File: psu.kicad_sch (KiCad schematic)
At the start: 68 parts, among them J3 Screw_Terminal_01x03, J4 Screw_Terminal_01x02, U11 LM337_SOT223, U14 LM337_SOT223, U15 AP1117-ADJ, U18 AP1117-ADJ, U2 AP1117-ADJ

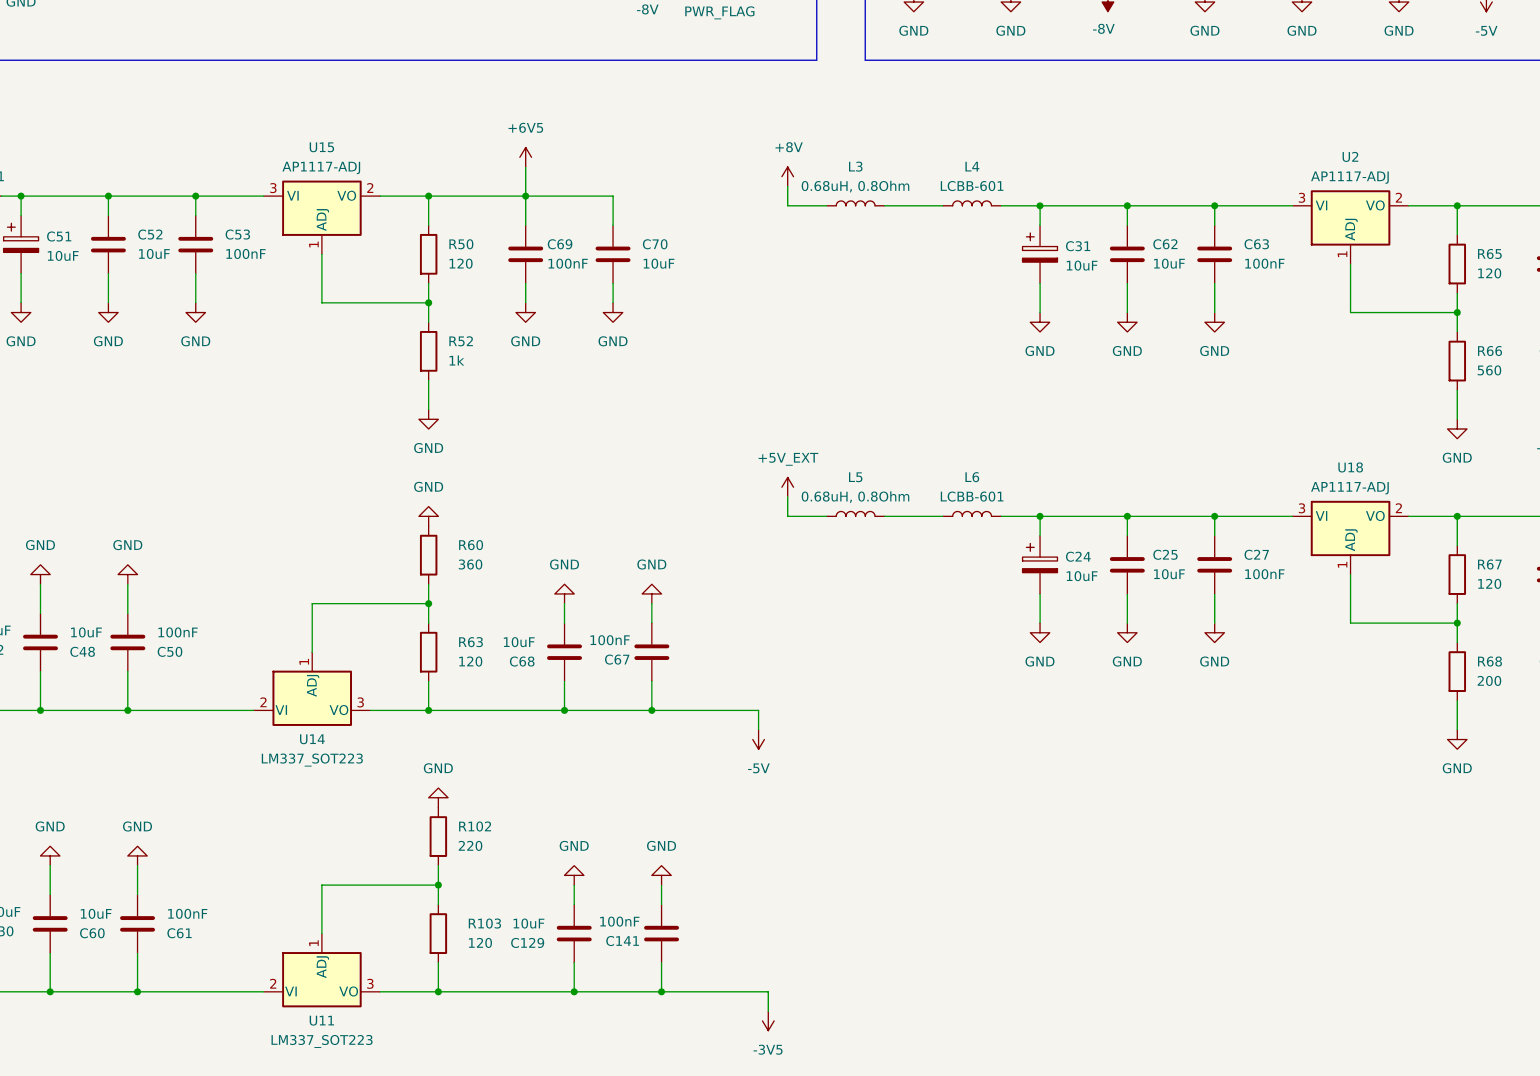
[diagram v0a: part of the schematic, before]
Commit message: Remove the stage between DAC and FET buffer
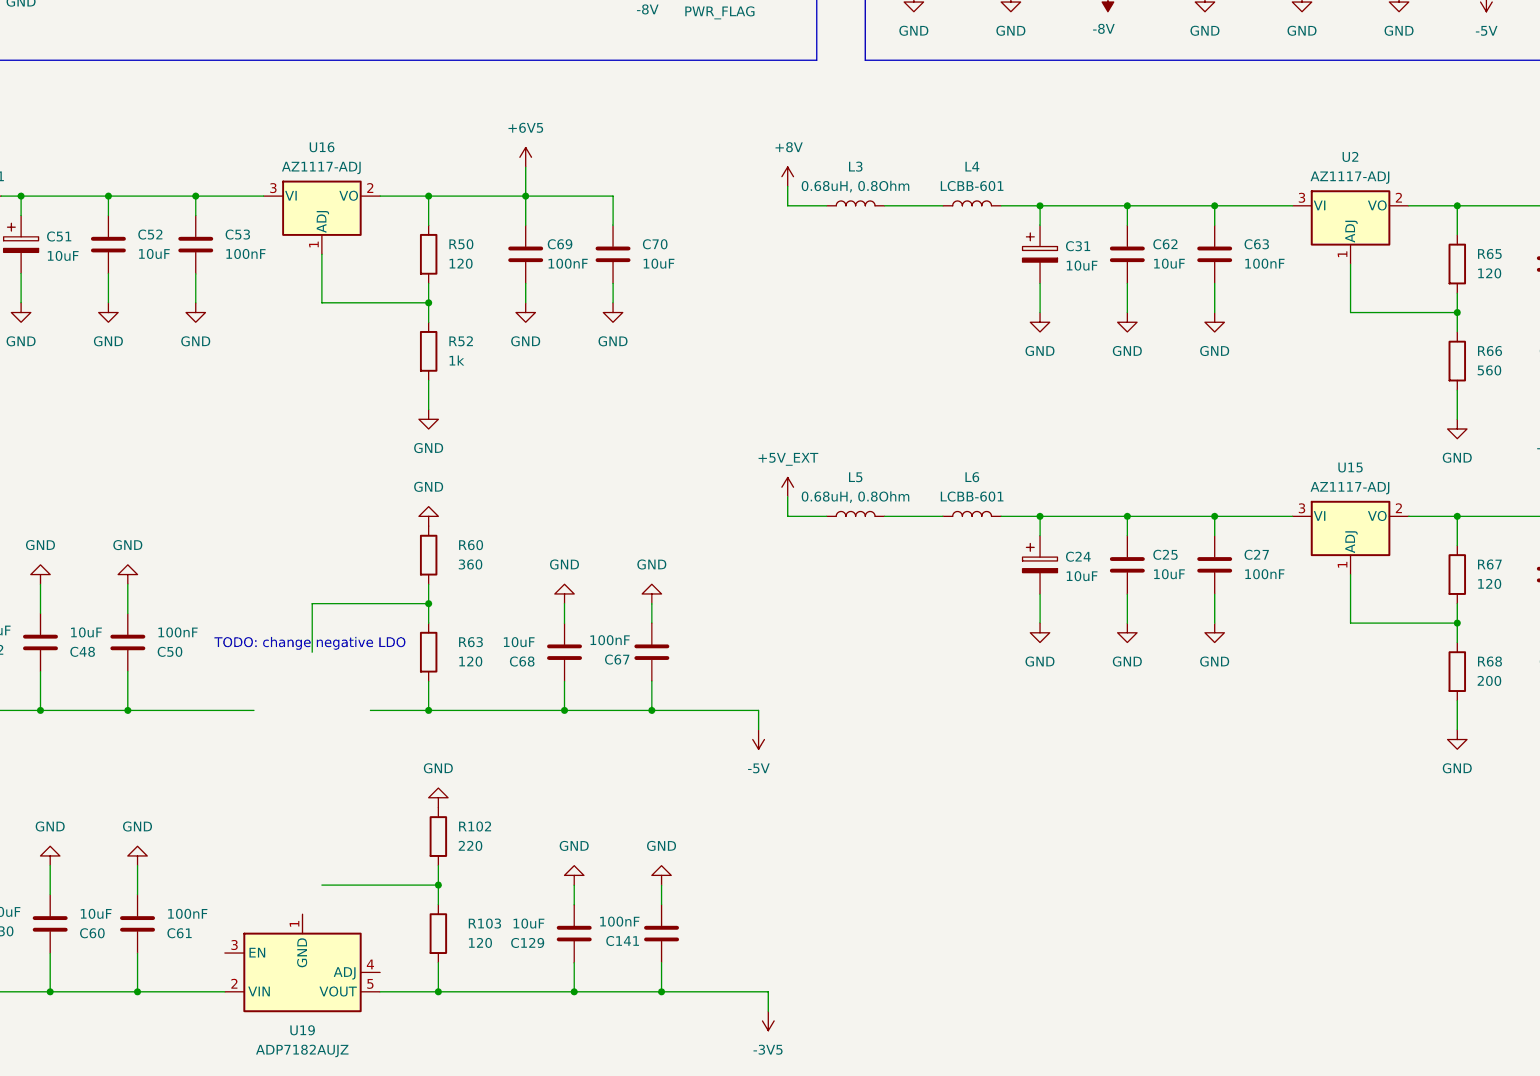
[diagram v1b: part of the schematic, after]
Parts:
- removed U11, U14: LM337_SOT223, Package_TO_SOT_SMD:SOT-223-3_TabPin2, symbol Regulator_Linear:LM337_SOT223
- removed U15, U18, U2: AP1117-ADJ, Package_TO_SOT_SMD:SOT-223-3_TabPin2, symbol Regulator_Linear:AP1117-ADJ
- added U15, U16, U2: AZ1117-ADJ, symbol Regulator_Linear:AZ1117-ADJ
- added U19: ADP7182AUJZ, Package_TO_SOT_SMD:TSOT-23-5, symbol Regulator_Linear:ADP7182AUJZ
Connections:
- net +3V3: now also U15.2 (VO)
- net +5V: now also U2.2 (VO)
- net +6V5: now also U16.2 (VO)
- net -3V5: now also U19.5 (VOUT)
- net at C31.1, C62.1, C63.1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: now also U2.3 (VI)
- net at R67.2, R68.1: now also U15.1 (ADJ)
- net at R65.2, R66.1: now also U2.1 (ADJ)
- net at C30.1, C60.1, C61.1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: now also U19.2 (VIN)
- net at C24.1, C25.1, C27.1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: now also U15.3 (VI)
- net at R50.2, R52.1: now also U16.1 (ADJ)
- net at C51.1, C52.1, C53.1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: now also U16.3 (VI)
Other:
- note added: "TODO: change negative LDO"

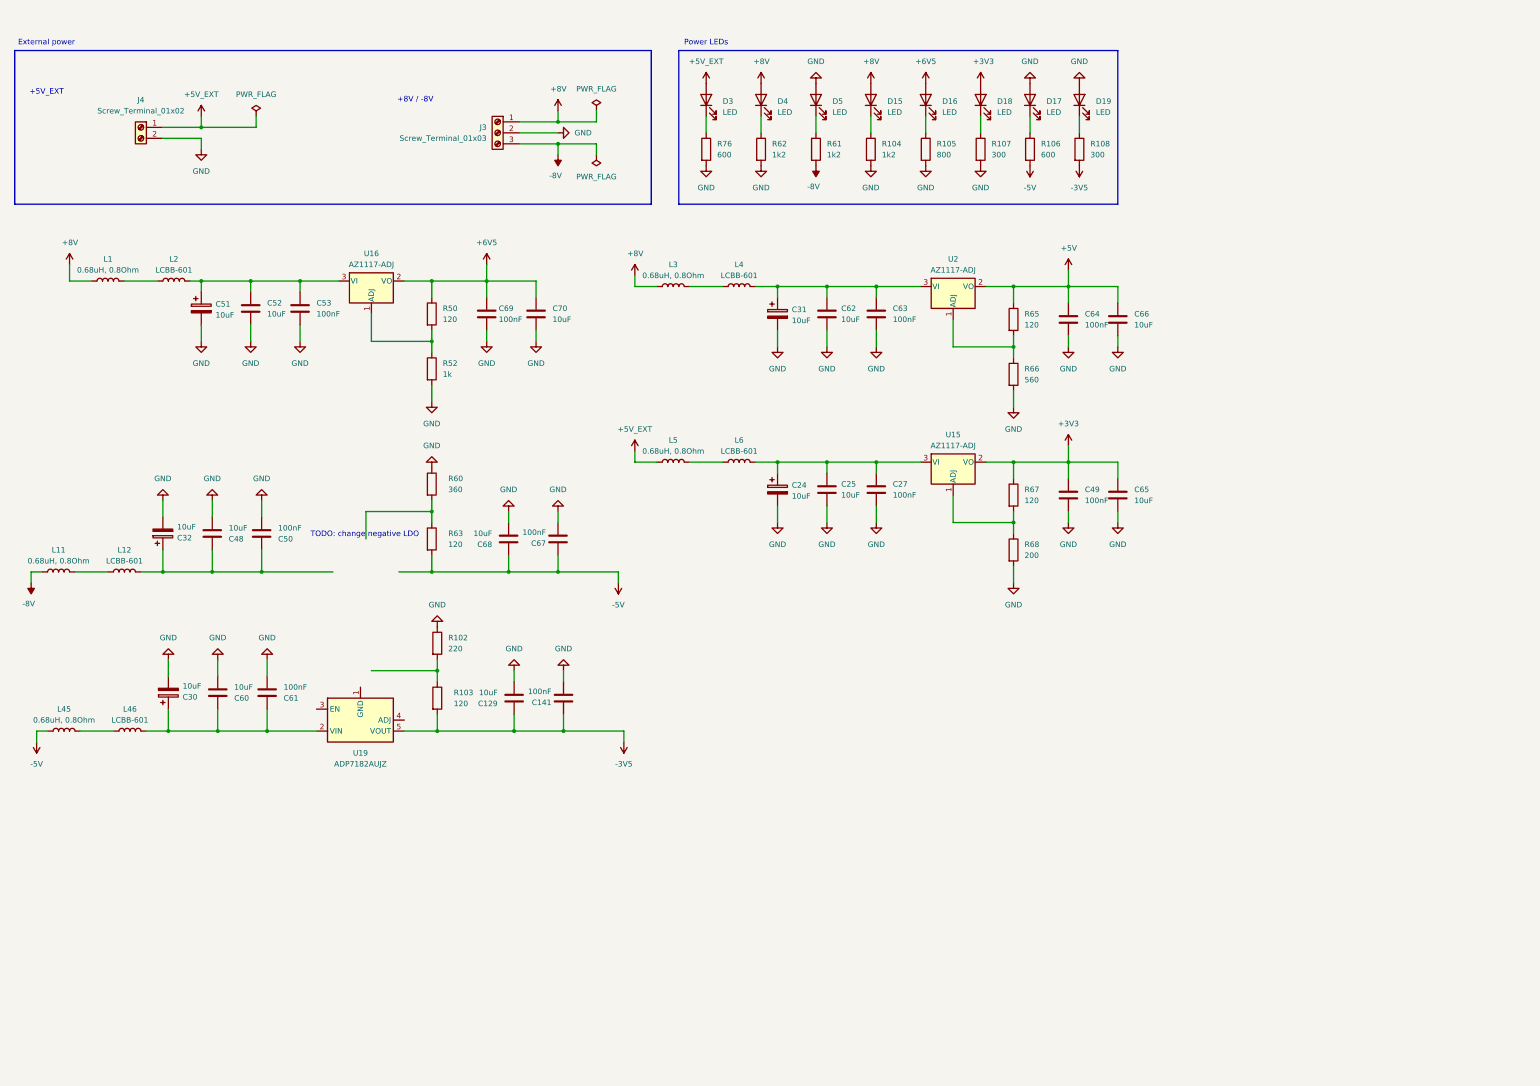
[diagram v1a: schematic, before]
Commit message: Finished up schematic? - Added missing PSU lines
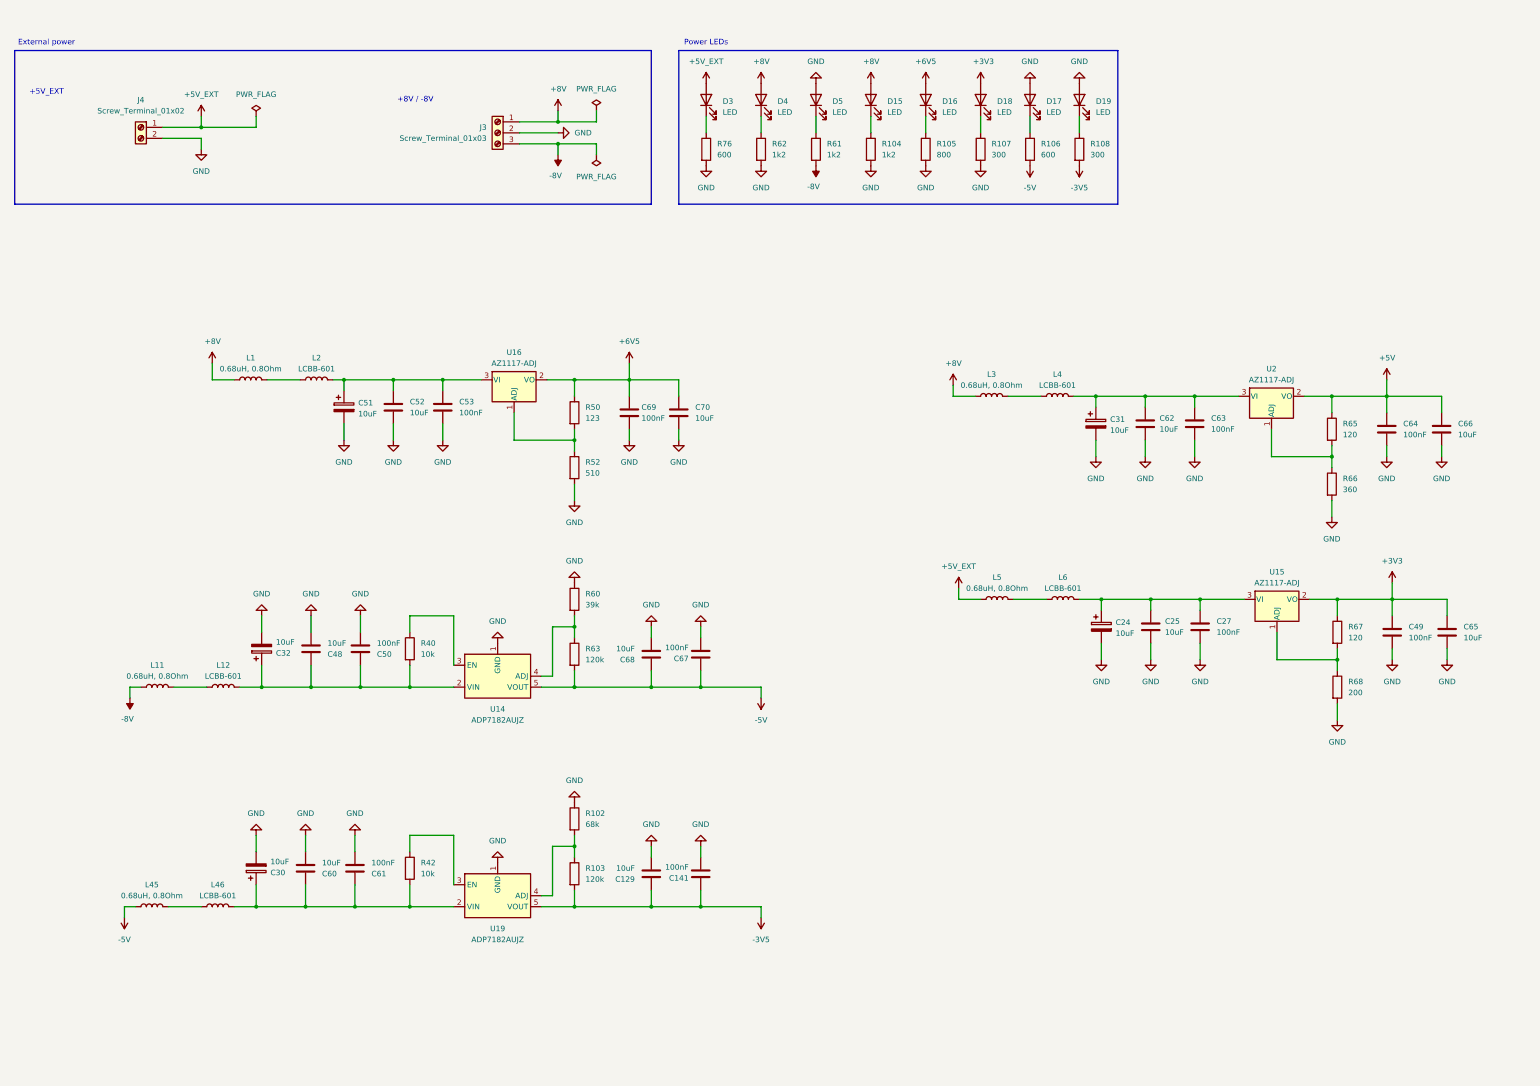
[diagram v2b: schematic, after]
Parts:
- added R40, R42: 10k, Resistor_SMD:R_0805_2012Metric, symbol Device:R
- added U14: ADP7182AUJZ, Package_TO_SOT_SMD:TSOT-23-5, symbol Regulator_Linear:ADP7182AUJZ
- R102: value 220 -> 68k
- R103, R63: value 120 -> 120k
- R50: value 120 -> 123
- R52: value 1k -> 510
- R60: value 360 -> 39k
- R66: value 560 -> 360
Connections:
- net -5V: now also U14.5 (VOUT)
- net GND: now also U19.1 (GND), U14.1 (GND)
- net at C32.1, C48.1, C50.1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: now also R40.2, U14.2 (VIN)
- net at R102.2, R103.1: now also U19.4 (ADJ)
- net at C30.1, C60.1, C61.1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: now also R42.2
- net at R60.2, R63.1: now also U14.4 (ADJ)
- net at U19.3 (EN): now also R42.1
- new net: R40.1, U14.3 (EN)
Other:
- note removed: "TODO: change negative LDO"
- moved on the sheet: C129, C141, C24, C25, C27, C30, C31, C32, C48, C49, C50, C51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

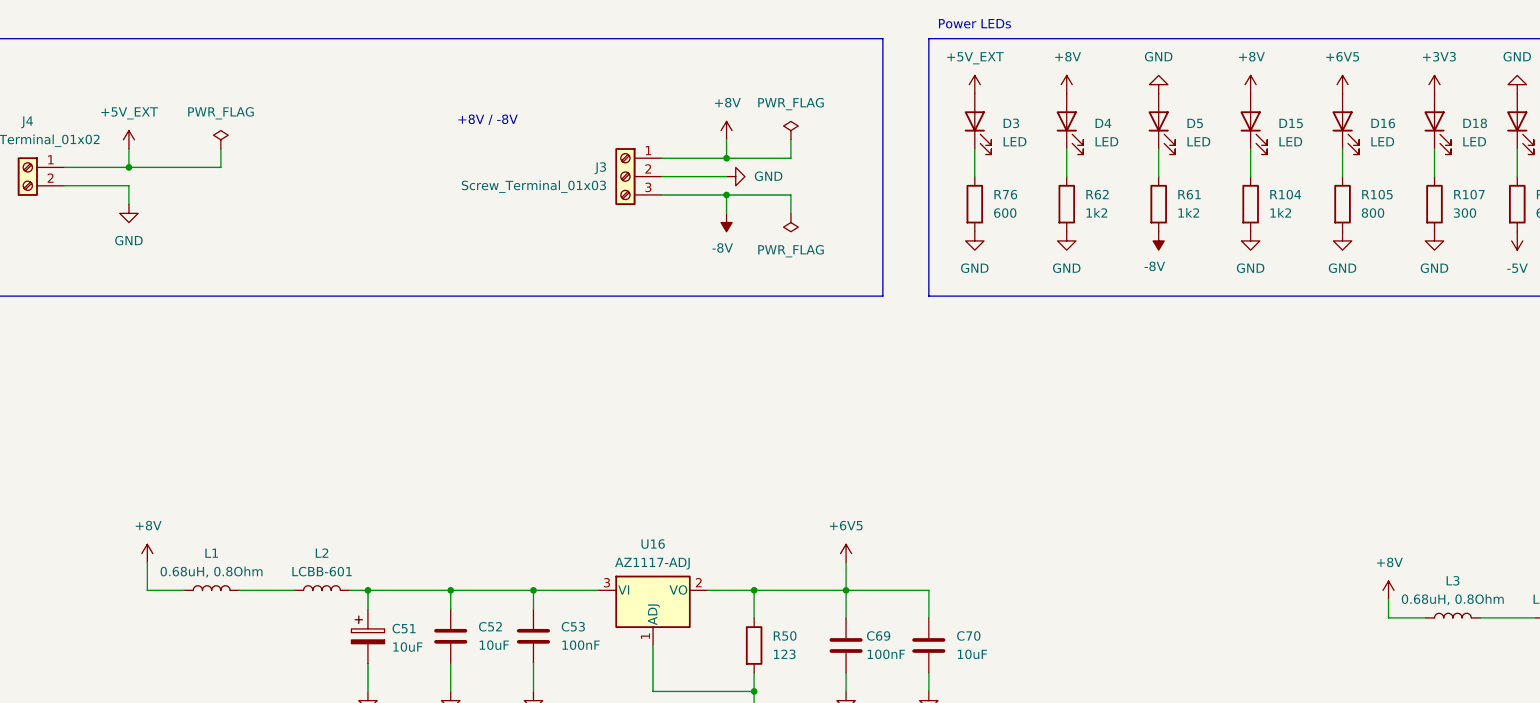
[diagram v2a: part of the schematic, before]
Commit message: Start working on ERC, properly annotate DNP elements
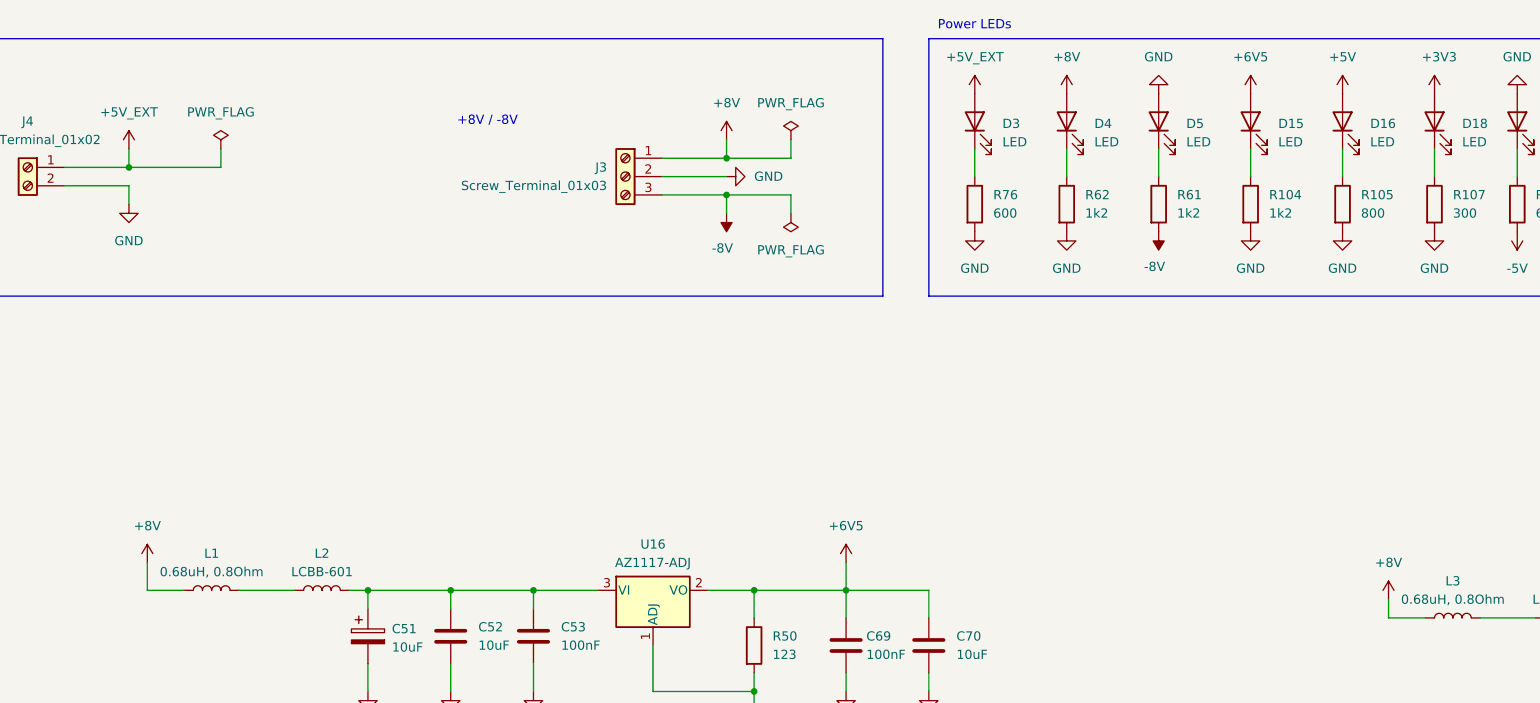
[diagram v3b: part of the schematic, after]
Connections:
- net +5V: now also D16.2 (A)
- net +6V5: now also D15.2 (A); no longer D16.2 (A)
- net +8V: no longer D15.2 (A)

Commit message: Add all footprints
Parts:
- D12: renamed from D3; footprint LED_SMD:LED_0805_2012Metric -> Diode_THT:D_DO-41_SOD81_P10.16mm_Horizontal
- D13: renamed from D4; footprint LED_SMD:LED_0805_2012Metric -> Diode_THT:D_DO-41_SOD81_P10.16mm_Horizontal
- D14: renamed from D5; footprint LED_SMD:LED_0805_2012Metric -> Diode_THT:D_DO-41_SOD81_P10.16mm_Horizontal
- J6: renamed from J4; footprint (none) -> TerminalBlock:TerminalBlock_MaiXu_MX126-5.0-02P_1x02_P5.00mm
- J7: renamed from J3; footprint (none) -> TerminalBlock:TerminalBlock_MaiXu_MX126-5.0-03P_1x03_P5.00mm
- L41: renamed from L45; footprint (none) -> Inductor_SMD:L_0805_2012Metric
- L42: renamed from L11; footprint (none) -> Inductor_SMD:L_0805_2012Metric
- L43: renamed from L46; footprint (none) -> Inductor_SMD:L_0805_2012Metric
- L44: renamed from L12; footprint (none) -> Inductor_SMD:L_0805_2012Metric
- L45: renamed from L1; footprint (none) -> Inductor_SMD:L_0805_2012Metric
- L46: renamed from L2; footprint (none) -> Inductor_SMD:L_0805_2012Metric
- L47: renamed from L3; footprint (none) -> Inductor_SMD:L_0805_2012Metric
- L48: renamed from L5; footprint (none) -> Inductor_SMD:L_0805_2012Metric
- L49: renamed from L4; footprint (none) -> Inductor_SMD:L_0805_2012Metric
- L50: renamed from L6; footprint (none) -> Inductor_SMD:L_0805_2012Metric
- U14: renamed from U16; footprint (none) -> Package_TO_SOT_SMD:SOT-89-3
- U15: renamed from U2; footprint (none) -> Package_TO_SOT_SMD:SOT-89-3
- U16: renamed from U15; footprint (none) -> Package_TO_SOT_SMD:SOT-89-3
- renumbered C30 to C101, C32 to C102, C60 to C103, C48 to C104, C51 to C105, C61 to C106, C50 to C107, C52 to C108, C53 to C109, C69 to C110, C68 to C111, C129 to C112, C70 to C113, C67 to C114, C141 to C115, C31 to C116, C24 to C117, C62 to C118, C25 to C119, C63 to C120, C27 to C121, C64 to C122, C49 to C123, C66 to C124, C65 to C125, D18 to D17, D17 to D18, R40 to R156, R42 to R157, R50 to R158, R52 to R159, R60 to R160, R63 to R161, R102 to R162, R103 to R163, R76 to R164, R62 to R165, R61 to R166, R104 to R167, R105 to R168, R107 to R169, R106 to R170, R108 to R171, R65 to R172, R66 to R173, R67 to R174, R68 to R175, U14 to U12, U19 to U13
